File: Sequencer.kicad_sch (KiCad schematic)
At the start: 44 parts, among them J1 Screw_Terminal_01x12, J2 USB_B_Micro, SW1 Mode, U1 ATtiny814-SS, U2 TLP3123, U3 TLP3123, U4 TLP3123, U5 TLP3123, U6 MC78L05_SOT89, U7 FT230XS

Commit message: Added MCU controlled LED Changed bottom fill to cover two resistors
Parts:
- added D9: PWR, LED_SMD:LED_0603_1608Metric, symbol Device:LED
- added R17: 1K, Resistor_SMD:R_0603_1608Metric, symbol Device:R_US
- D3: value IR26-21C_L110_TR8 -> SEQ3
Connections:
- net GND: now also D9.1 (K)
- net LED: now also R17.1
- new net: D9.2 (A), R17.2
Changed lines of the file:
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@@
 	(wire
 		(pts
+			(xy 121.92 105.41) (xy 121.92 106.68)
+		)
+		(stroke
+			(width 0)
+			(type default)
+		)
+	)
+	(wire
+		(pts
 			(xy 110.49 177.8) (xy 102.87 177.8)
 		)
@@
 	(wire
 		(pts
+			(xy 119.38 96.52) (xy 121.92 96.52)
+		)
+		(stroke
+			(width 0)
+			(type default)
+		)
+	)
+	(wire
+		(pts
 			(xy 212.09 113.03) (xy 223.52 113.03)
 		)
@@
 	(wire
 		(pts
-			(xy 99.06 96.52) (xy 110.49 96.52)
+			(xy 99.06 96.52) (xy 111.76 96.52)
 		)
 		(stroke
@@
 	(wire
 		(pts
+			(xy 121.92 96.52) (xy 121.92 97.79)
+		)
+		(stroke
+			(width 0)
+			(type default)
+		)
+	)
+	(wire
+		(pts
 			(xy 182.88 106.68) (xy 182.88 113.03)
 		)
@@
 		)
 	)
-	(label "RST\\"
-		(at 63.5 172.72 0)
-		(fields_autoplaced yes)
-		(effects
-			(font
-				(size 1.27 1.27)
-			)
-			(justify left bottom)
-		)
-	)
-	(label "VCCIO"
-		(at 81.28 146.05 0)
-		(fields_autoplaced yes)
-		(effects
-			(font
-				(size 1.27 1.27)
-			)
-			(justify left bottom)
-		)
-	)
 	(label "D-M"
 		(at 62.23 165.1 0)
@@
 	)
 	(symbol
+		(lib_id "Device:LED")
+		(at 121.92 101.6 90)
+		(unit 1)
+		(exclude_from_sim no)
+		(in_bom yes)
+		(on_board yes)
+		(dnp no)
+		(property "Reference" "D9"
+			(at 118.11 101.6 90)
+			(effects
+				(font
+					(size 1.27 1.27)
+				)
+			)
+		)
+		(property "Value" "PWR"
+			(at 126.238 101.6 90)
+			(effects
+				(font
+					(size 1.27 1.27)
+				)
+			)
+		)
+		(property "Footprint" "LED_SMD:LED_0603_1608Metric"
+			(at 121.92 101.6 0)
+			(effects
+				(font
+					(size 1.27 1.27)
+				)
+				(hide yes)
+			)
+		)
+		(property "Datasheet" "~"
+			(at 121.92 101.6 0)
+			(effects
+				(font
+					(size 1.27 1.27)
+				)
+				(hide yes)
+			)
+		)
+		(property "Description" "Light emitting diode"
+			(at 121.92 101.6 0)
+			(effects
+				(font
+					(size 1.27 1.27)
+				)
+				(hide yes)
+			)
+		)
+		(pin "2"
+		)
+		(pin "1"
+		)
+		(instances
+			(project "Sequencer"
+				(path "/3f7e4896-a5a1-43ac-9348-16f0feb459b4"
+					(reference "D9")
+					(unit 1)
+				)
+			)
+		)
+	)
+	(symbol
 		(lib_id "LED:IR26-21C_L110_TR8")
 		(at 204.47 147.32 180)
@@
 	(symbol
 		(lib_id "power:GND")
+		(at 121.92 106.68 0)
+		(unit 1)
+		(exclude_from_sim no)
+		(in_bom yes)
+		(on_board yes)
+		(dnp no)
+		(fields_autoplaced yes)
+		(property "Reference" "#PWR027"
+			(at 121.92 113.03 0)
+			(effects
+				(font
+					(size 1.27 1.27)
+				)
+				(hide yes)
+			)
+		)
+		(property "Value" "GND"
+			(at 121.92 111.76 0)
+			(effects
+				(font
+					(size 1.27 1.27)
+				)
+				(hide yes)
+			)
+		)
+		(property "Footprint" ""
+			(at 121.92 106.68 0)
+			(effects
+				(font
+					(size 1.27 1.27)
+				)
+				(hide yes)
+			)
+		)
+		(property "Datasheet" ""
+			(at 121.92 106.68 0)
+			(effects
+				(font
+					(size 1.27 1.27)
+				)
+				(hide yes)
+			)
+		)
+		(property "Description" "Power symbol creates a global label with name \"GND\" , ground"
+			(at 121.92 106.68 0)
+			(effects
+				(font
+					(size 1.27 1.27)
+				)
+				(hide yes)
+			)
+		)
+		(pin "1"
+		)
+		(instances
+			(project "Sequencer"
+				(path "/3f7e4896-a5a1-43ac-9348-16f0feb459b4"
+					(reference "#PWR027")
+					(unit 1)
+				)
+			)
+		)
+	)
+	(symbol
+		(lib_id "power:GND")
 		(at 20.32 163.83 0)
 		(unit 1)
@@
 	(symbol
 		(lib_id "Device:R_US")
+		(at 115.57 96.52 90)
+		(mirror x)
+		(unit 1)
+		(exclude_from_sim no)
+		(in_bom yes)
+		(on_board yes)
+		(dnp no)
+		(property "Reference" "R17"
+			(at 114.046 93.98 90)
+			(effects
+				(font
+					(size 1.27 1.27)
+				)
+			)
+		)
+		(property "Value" "1K"
+			(at 118.364 93.98 90)
+			(effects
+				(font
+					(size 1.27 1.27)
+				)
+			)
+		)
+		(property "Footprint" "Resistor_SMD:R_0603_1608Metric"
+			(at 115.824 97.536 90)
+			(effects
+				(font
+					(size 1.27 1.27)
+				)
+				(hide yes)
+			)
+		)
+		(property "Datasheet" "~"
+			(at 115.57 96.52 0)
+			(effects
+				(font
+					(size 1.27 1.27)
+				)
+				(hide yes)
+			)
+		)
+		(property "Description" "Resistor, US symbol"
+			(at 115.57 96.52 0)
+			(effects
+				(font
+					(size 1.27 1.27)
+				)
+				(hide yes)
+			)
+		)
+		(pin "1"
+		)
+		(pin "2"
+		)
+		(instances
+			(project "Sequencer"
+				(path "/3f7e4896-a5a1-43ac-9348-16f0feb459b4"
+					(reference "R17")
+					(unit 1)
+				)
+			)
+		)
+	)
+	(symbol
+		(lib_id "Device:R_US")
 		(at 191.77 134.62 90)
 		(mirror x)
@@
 			)
 		)
-		(property "Value" "IR26-21C_L110_TR8"
+		(property "Value" "SEQ3"
 			(at 206.0575 123.19 0)
 			(effects

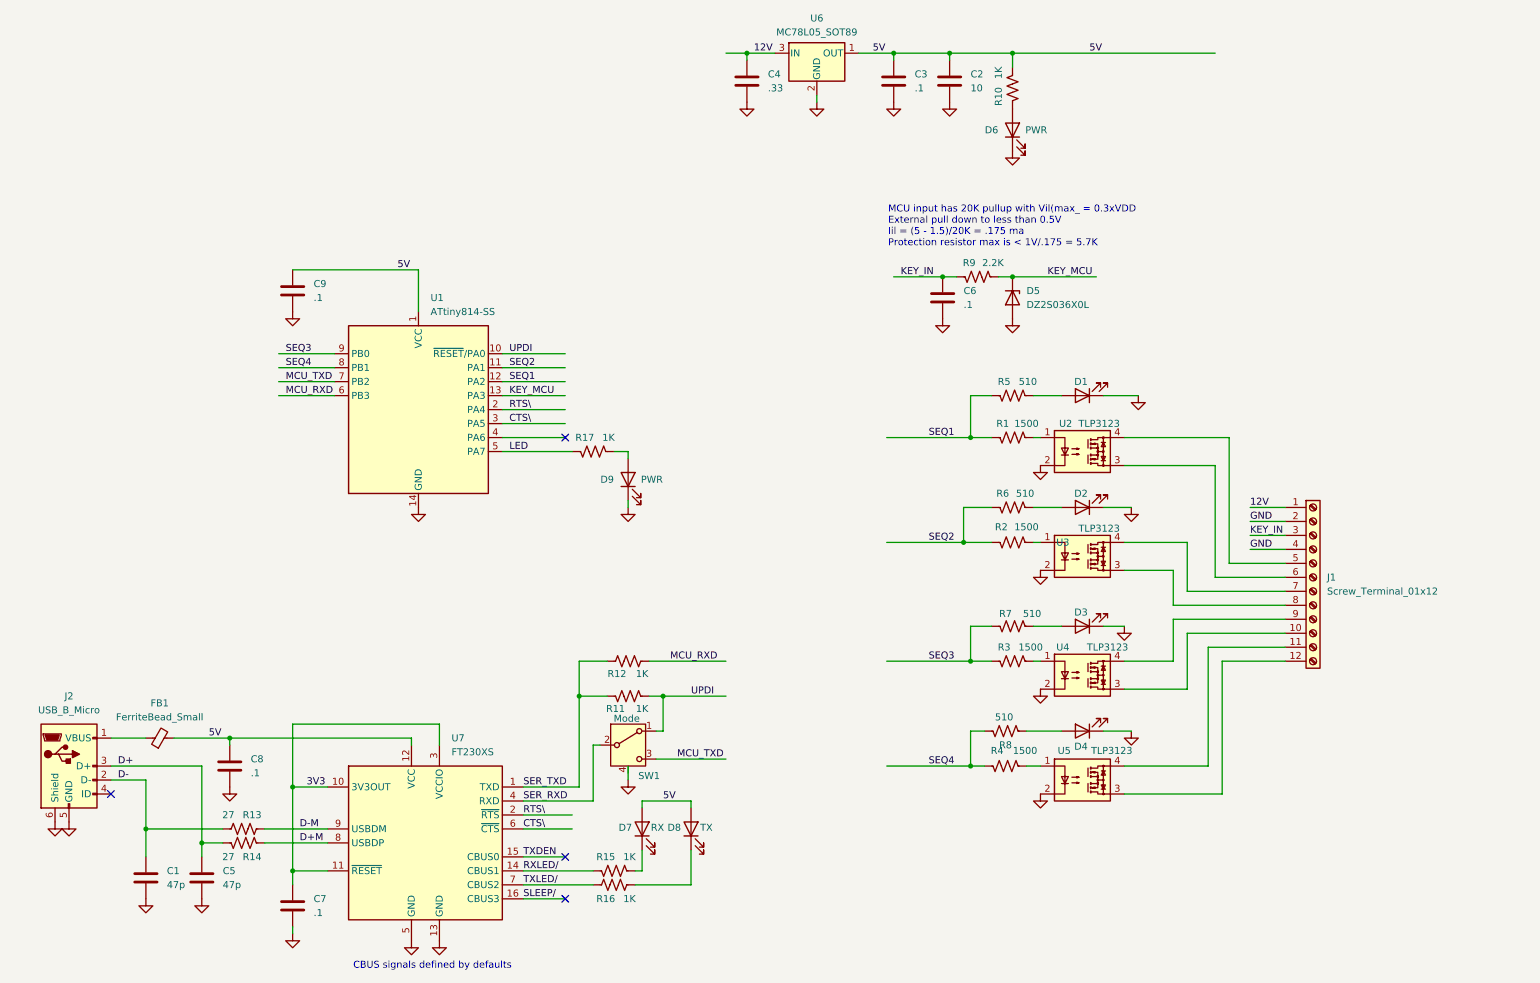
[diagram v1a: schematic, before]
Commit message: Converted to USB-C connector Added zener protection to USB data wires Shuffled layout to reduce jumpers Generated BOM and gerbers for experimenting with JLCPCB
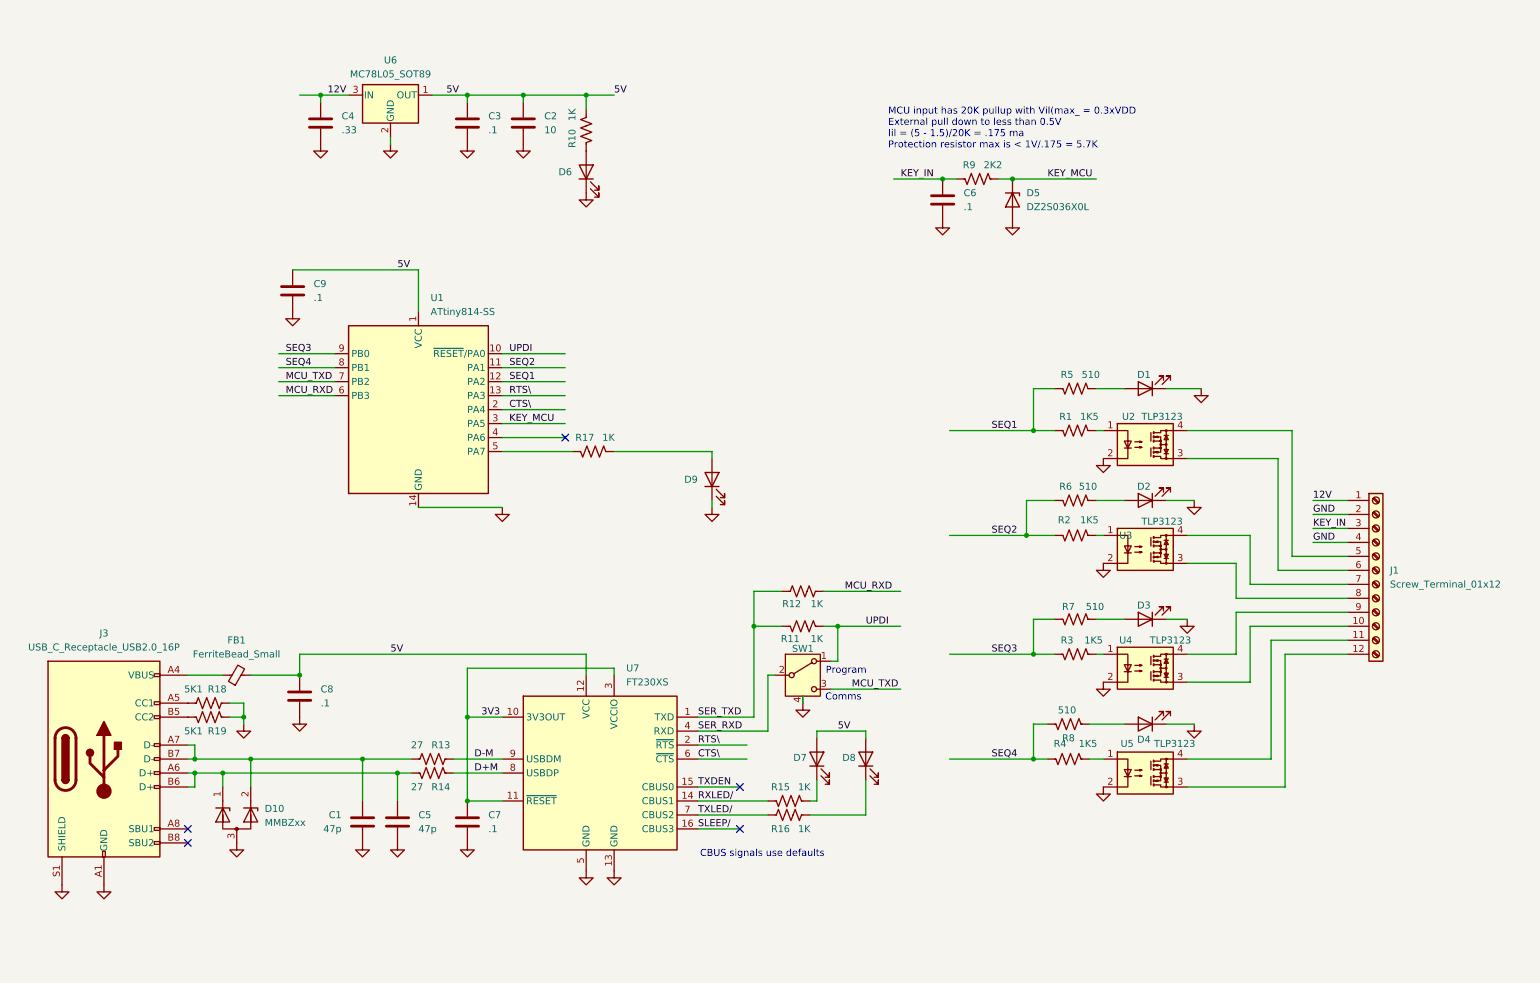
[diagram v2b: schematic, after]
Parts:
- removed J2: USB_B_Micro, Connector_USB:USB_Micro-B_Amphenol_10103594-0001LF_Horizontal, symbol Connector:USB_B_Micro
- added D10: MMBZxx, Package_TO_SOT_SMD:SOT-23, symbol Diode:MMBZxx
- added J3: USB_C_Receptacle_USB2.0_16P, Connector_USB:USB_C_Receptacle_G-Switch_GT-USB-7010ASV, symbol Connector:USB_C_Receptacle_USB2.0_16P
- added R18, R19: 5K1, Resistor_SMD:R_0603_1608Metric, symbol Device:R_US
- D1, D2, D4: value IR26-21C_L110_TR8 -> Red
- D3: value SEQ3 -> Red
- D6, D9: value PWR -> Green
- D7: value RX -> Yellow
- D8: value TX -> Yellow
- R1, R2, R3, R4: value 1500 -> 1K5
- R9: value 2.2K -> 2K2
- SW1: value Mode -> Switch
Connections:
- net CTS\: now also U1.2 (PA4); no longer U1.3 (PA5)
- net GND: now also D10.3 (A), J3.A1 (GND), J3.A12 (GND), J3.B1 (GND), J3.B12 (GND), J3.S1 (SHIELD), R18.1, R19.1
- net KEY_MCU: now also U1.3 (PA5); no longer U1.13 (PA3)
- net RTS\: now also U1.13 (PA3); no longer U1.2 (PA4)
- net at FB1.1: now also J3.A4 (VBUS), J3.A9 (VBUS), J3.B4 (VBUS), J3.B9 (VBUS)
- net D+: no longer names the net of C5.1, R14.2
- net D+: now also D10.1 (K), J3.A6 (D+), J3.B6 (D+)
- net D-: no longer names the net of C1.1, R13.2
- net D-: now also D10.2 (K), J3.A7 (D-), J3.B7 (D-)
- net LED: no longer names the net of R17.1, U1.5 (PA7)
- new net: J3.A5 (CC1), R18.2
- new net: J3.B5 (CC2), R19.2
- no-connect marks 4 -> 5
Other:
- note added: "CBUS signals use defaults"
- note added: "Comms"
- note added: "Program"
- note removed: "CBUS signals defined by defaults"
- moved on the sheet: C1, C2, C3, C4, C5, C6, C7, C8, D1, D2, D3, D4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

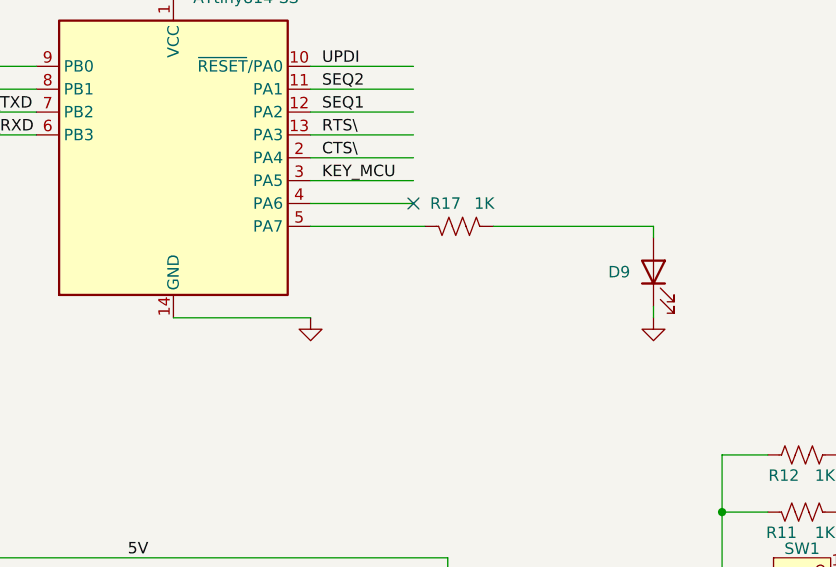
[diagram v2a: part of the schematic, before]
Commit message: middle of trying to remove some jumpers and make wiring more direct Trying to create room for reverse polarity protection on 12V
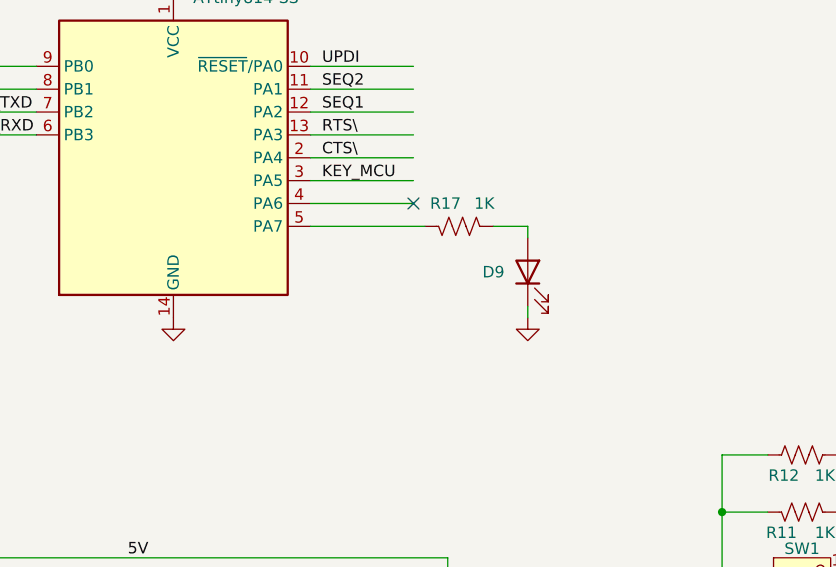
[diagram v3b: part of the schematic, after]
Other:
- moved on the sheet: D9
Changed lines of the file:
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@@
 	(wire
 		(pts
-			(xy 99.06 106.68) (xy 83.82 106.68)
-		)
-		(stroke
-			(width 0)
-			(type default)
-		)
-	)
-	(wire
-		(pts
 			(xy 92.71 160.02) (xy 92.71 144.78)
 		)
@@
 	(wire
 		(pts
-			(xy 137.16 105.41) (xy 137.16 106.68)
+			(xy 123.19 105.41) (xy 123.19 106.68)
 		)
 		(stroke
@@
 	(wire
 		(pts
-			(xy 119.38 96.52) (xy 137.16 96.52)
-		)
-		(stroke
-			(width 0)
-			(type default)
-		)
-	)
-	(wire
-		(pts
 			(xy 223.52 111.76) (xy 234.95 111.76)
 		)
@@
 	(wire
 		(pts
+			(xy 119.38 96.52) (xy 123.19 96.52)
+		)
+		(stroke
+			(width 0)
+			(type default)
+		)
+	)
+	(wire
+		(pts
 			(xy 252.73 130.81) (xy 238.76 130.81)
 		)
@@
 	(wire
 		(pts
-			(xy 137.16 96.52) (xy 137.16 97.79)
+			(xy 123.19 96.52) (xy 123.19 97.79)
 		)
 		(stroke
@@
 	(symbol
 		(lib_id "Device:LED")
-		(at 137.16 101.6 90)
+		(at 123.19 101.6 90)
 		(unit 1)
 		(exclude_from_sim no)
@@
 		(dnp no)
 		(property "Reference" "D9"
-			(at 133.35 101.6 90)
+			(at 119.38 101.6 90)
 			(effects
 				(font
@@
 		)
 		(property "Value" "Green"
-			(at 141.478 101.6 90)
+			(at 127.508 101.6 90)
 			(effects
 				(font
@@
 		)
 		(property "Footprint" "LED_SMD:LED_0603_1608Metric"
-			(at 137.16 101.6 0)
+			(at 123.19 101.6 0)
 			(effects
 				(font
@@
 		)
 		(property "Datasheet" "~"
-			(at 137.16 101.6 0)
+			(at 123.19 101.6 0)
 			(effects
 				(font
@@
 		)
 		(property "Description" "Light emitting diode"
-			(at 137.16 101.6 0)
+			(at 123.19 101.6 0)
 			(effects
 				(font
@@
 	(symbol
 		(lib_id "power:GND")
-		(at 137.16 106.68 0)
+		(at 123.19 106.68 0)
 		(unit 1)
 		(exclude_from_sim no)
@@
 		(fields_autoplaced yes)
 		(property "Reference" "#PWR027"
-			(at 137.16 113.03 0)
+			(at 123.19 113.03 0)
 			(effects
 				(font
@@
 		)
 		(property "Value" "GND"
-			(at 137.16 111.76 0)
+			(at 123.19 111.76 0)
 			(effects
 				(font
@@
 		)
 		(property "Footprint" ""
-			(at 137.16 106.68 0)
+			(at 123.19 106.68 0)
 			(effects
 				(font
@@
 		)
 		(property "Datasheet" ""
-			(at 137.16 106.68 0)
+			(at 123.19 106.68 0)
 			(effects
 				(font
@@
 		)
 		(property "Description" "Power symbol creates a global label with name \"GND\" , ground"
-			(at 137.16 106.68 0)
+			(at 123.19 106.68 0)
 			(effects
 				(font
@@
 	(symbol
 		(lib_id "power:GND")
-		(at 99.06 106.68 0)
+		(at 83.82 106.68 0)
 		(unit 1)
 		(exclude_from_sim no)
@@
 		(fields_autoplaced yes)
 		(property "Reference" "#PWR02"
-			(at 99.06 113.03 0)
+			(at 83.82 113.03 0)
 			(effects
 				(font
@@
 		)
 		(property "Value" "GND"
-			(at 99.06 111.76 0)
+			(at 83.82 111.76 0)
 			(effects
 				(font
@@
 		)
 		(property "Footprint" ""
-			(at 99.06 106.68 0)
+			(at 83.82 106.68 0)
 			(effects
 				(font
@@
 		)
 		(property "Datasheet" ""
-			(at 99.06 106.68 0)
+			(at 83.82 106.68 0)
 			(effects
 				(font
@@
 		)
 		(property "Description" "Power symbol creates a global label with name \"GND\" , ground"
-			(at 99.06 106.68 0)
+			(at 83.82 106.68 0)
 			(effects
 				(font
